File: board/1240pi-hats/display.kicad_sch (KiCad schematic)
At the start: 6 parts, among them J10 Conn_02x05_Odd_Even, J11 Conn_01x03, P10 74HC74, U10 74HC74, U11 MC74VHC1G125, U12 MC74VHC1G125

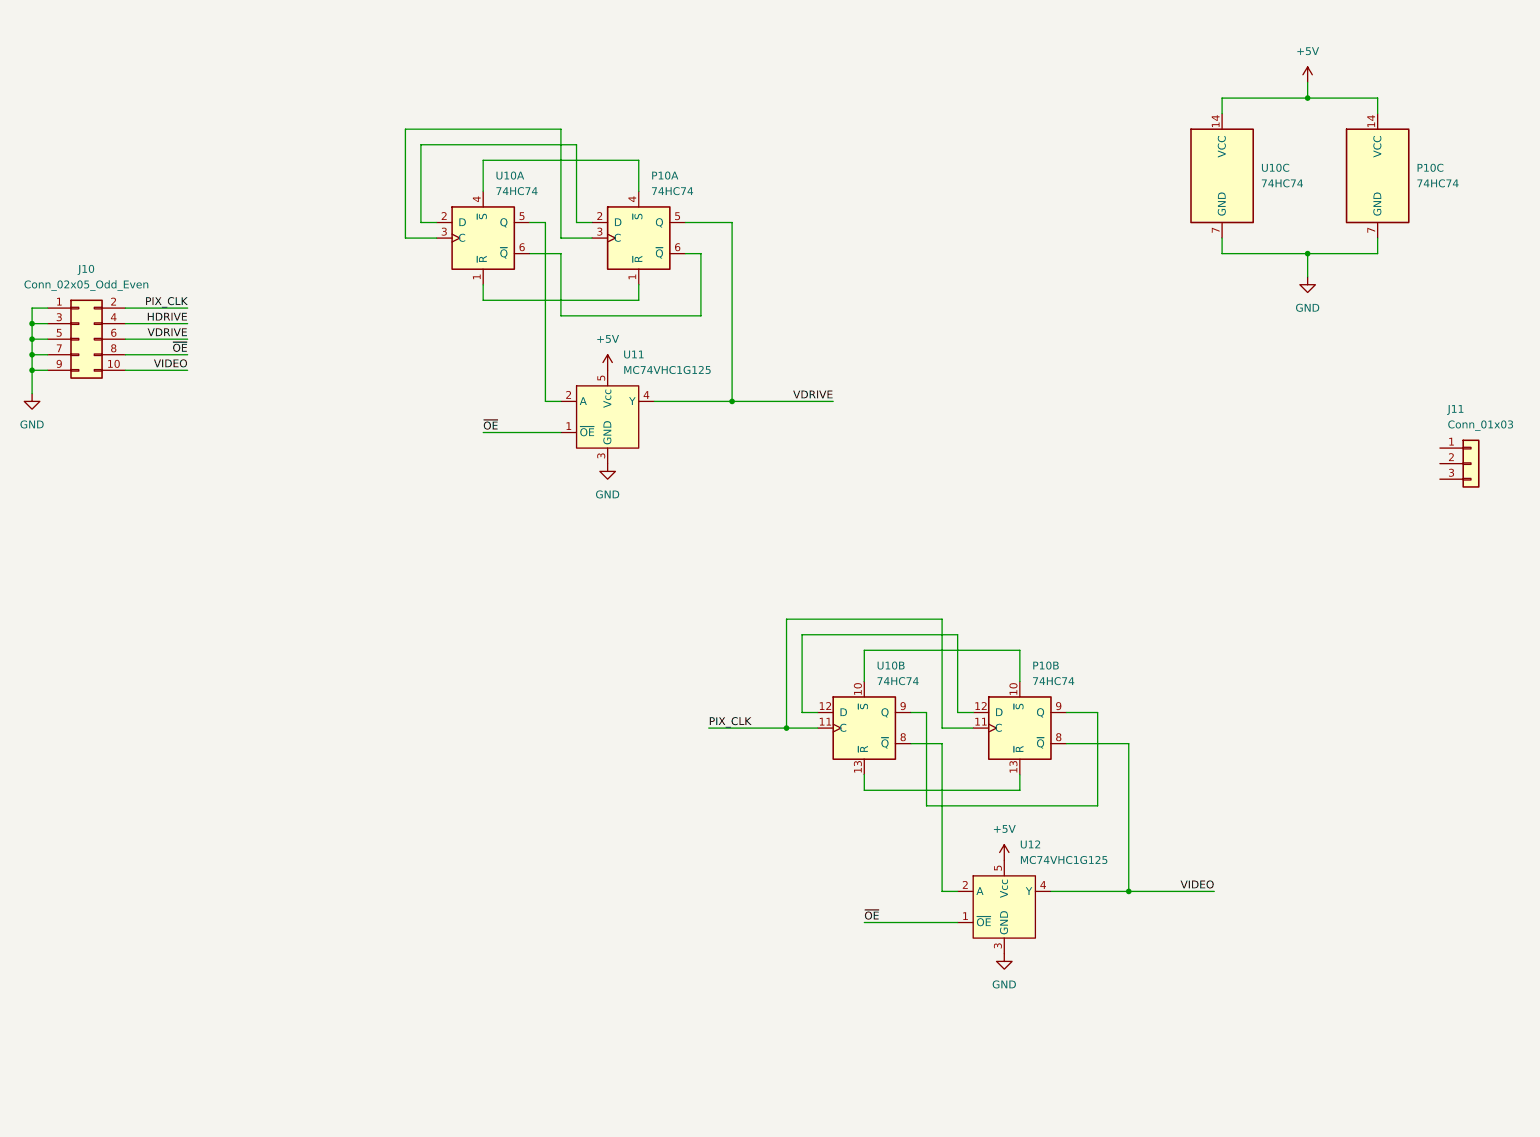
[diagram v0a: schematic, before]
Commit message: Redesign display hat to use a single board.
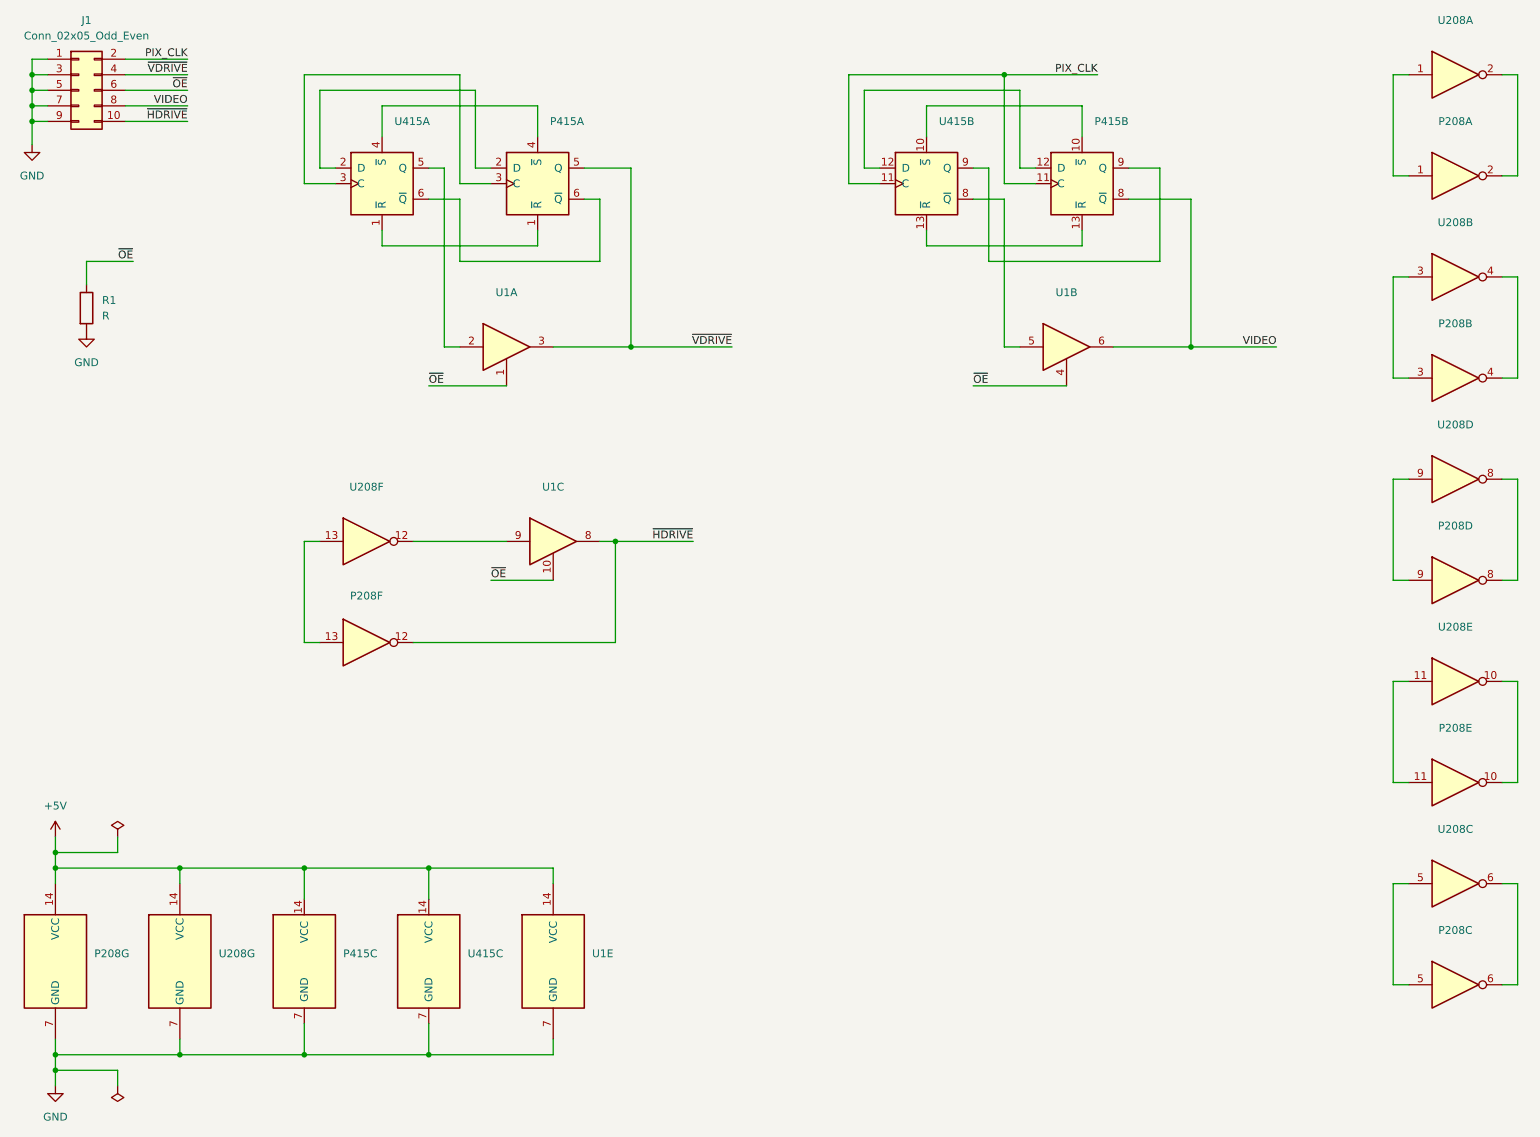
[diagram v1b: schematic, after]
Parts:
- removed J10: Conn_02x05_Odd_Even, symbol Connector_Generic:Conn_02x05_Odd_Even
- removed J11: Conn_01x03, symbol Connector_Generic:Conn_01x03
- removed P10, U10: 74HC74, symbol 74xx:74HC74
- removed U11, U12: MC74VHC1G125, symbol 0Local:MC74VHC1G125
- added J1: Conn_02x05_Odd_Even, Connector_PinHeader_2.54mm:PinHeader_2x05_P2.54mm_Vertical, symbol Connector_Generic:Conn_02x05_Odd_Even
- added P208, U208: (no value), Package_DIP:DIP-14_W7.62mm, symbol 74xx:74HC04
- added P415: (no value), Package_DIP:DIP-14_W7.62mm, symbol 74xx:74HC74
- added R1: R, symbol Device:R
- added U1: (no value), symbol 74xx:74LS126
- added U415: (no value), symbol 74xx:74HC74
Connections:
- net +5V: now also P208.14 (VCC), P415.14 (VCC), U1.14 (VCC), U208.14 (VCC), U415.14 (VCC)
- net GND: now also J1.1 (Pin_1), J1.3 (Pin_3), J1.5 (Pin_5), J1.7 (Pin_7), J1.9 (Pin_9), P208.7 (GND), P415.7 (GND), R1.2, U1.7 (GND), U208.7 (GND), U415.7 (GND)
- net PIX_CLK: now also J1.2 (Pin_2), P415.11 (C), U415.11 (C)
- net VIDEO: now also J1.8 (Pin_8), P415.8 (~{Q}), U1.6
- net ~{OE}: now also J1.6 (Pin_6), R1.1, U1.1, U1.10, U1.4
- new net: P208.10, U208.10
- new net: P208.11, U208.11
- new net: P208.5, U208.5
- new net: P208.6, U208.6
- new net: P208.8, U208.8
- new net: P208.9, U208.9
- new net: P415.10 (~{S}), U415.10 (~{S})
- new net: P415.12 (D), U415.12 (D)
- new net: P415.13 (~{R}), U415.13 (~{R})
- new net: P415.9 (Q), U415.9 (Q)
- new net: P208.13, U208.13
- new net: P208.3, U208.3
- new net: P208.4, U208.4
- new net: U1.9, U208.12
- new net: P415.1 (~{R}), U415.1 (~{R})
- new net: P415.2 (D), U415.2 (D)
- new net: P415.3 (C), U415.3 (C)
- new net: P415.4 (~{S}), U415.4 (~{S})
- new net: U1.2, U415.5 (Q)
- new net: P415.6 (~{Q}), U415.6 (~{Q})
- new net: P208.1, U208.1
- new net: P208.2, U208.2
- new net: U1.5, U415.8 (~{Q})
- new net ~{HDRIVE}: J1.10 (Pin_10), P208.12, U1.8
- new net ~{VDRIVE}: J1.4 (Pin_4), P415.5 (Q), U1.3

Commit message: Finish up display hat board.
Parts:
- added unit 4 of U1
- R1: value R -> (none)
- U208: footprint Package_DIP:DIP-14_W7.62mm -> (none)
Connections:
- net +5V: now also R1.1
- net GND: now also U1.12, U1.13; no longer R1.2
- net PIX_CLK: now also J1.4 (Pin_4); no longer J1.2 (Pin_2)
- net VIDEO: now also J1.6 (Pin_6), U1.3; no longer J1.8 (Pin_8), U1.6
- net ~{HDRIVE}: now also J1.8 (Pin_8); no longer J1.10 (Pin_10)
- net ~{VDRIVE}: now also J1.10 (Pin_10), U1.6; no longer J1.4 (Pin_4), U1.3
- net at U415.5 (Q): now also U1.5; no longer U1.2
- net at U415.8 (~{Q}): now also U1.2; no longer U1.5
- net ~{OE} renamed ~{EXT_EN}
- net ~{EXT_EN}: now also J1.2 (Pin_2), R1.2; no longer J1.6 (Pin_6), R1.1
- no-connect marks 0 -> 1
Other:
- moved on the sheet: R1, U1A, U1B

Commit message: Add IO Processor hat board.
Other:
- company: (none) -> © 2022 Sam Hanes, licensed under CERN-OHL-P v2
- title: (none) -> 1240-Pi Modification Boards
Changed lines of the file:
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@@
 (kicad_sch (version 20211123) (generator eeschema)
   (paper "USLetter")
+  (title_block
+    (title "1240-Pi Modification Boards")
+    (date "2022-04-21")
+    (rev "1.0")
+    (company "© 2022 Sam Hanes, licensed under CERN-OHL-P v2")
+    (comment 1 "https://github.com/Elemecca/1240pi")
+  )
   (junction (at 22.86 187.96) (diameter 0) (color 0 0 0 0)
   )
@@
   (symbol (lib_id "power:GND") (at 175.26 123.19 0) (unit 1)
     (in_bom yes) (on_board yes) (fields_autoplaced)
-    (property "Reference" "#PWR?" (id 0) (at 175.26 129.54 0)
-      (effects (font (size 1.27 1.27)) hide)
-    )
+    (property "Reference" "#PWR0105" (id 0) (at 175.26 129.54 0)
+      (effects (font (size 1.27 1.27)) hide)
+    )
